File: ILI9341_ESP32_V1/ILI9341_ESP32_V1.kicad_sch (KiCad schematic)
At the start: 72 parts, among them J1 USB_C_Receptacle_USB2.0_16P, J2 Conn_01x02_Female, J3 Conn_01x02_Female, J4 Conn_01x18_Socket, Q1 BC807, SW1 SW_DIP_x01, SW10 SW_Push, SW11 SW_Push, SW12 SW_Push, SW13 SW_Wuerth_450301014042, SW2 SW_Push, SW3 SW_Push, SW4 SW_Push, SW5 SW_Push, SW6 SW_Push, SW7 SW_Push, SW8 SW_Push, SW9 SW_Push, U1 MCP73831-2-OT, U2 XM5062S, U3 ESP32-S3-WROOM-2, U4 3_2_ZOLL_ILI9341, U5 MAX98357AETE+T, U6 02FVS3, U7 02FVS3

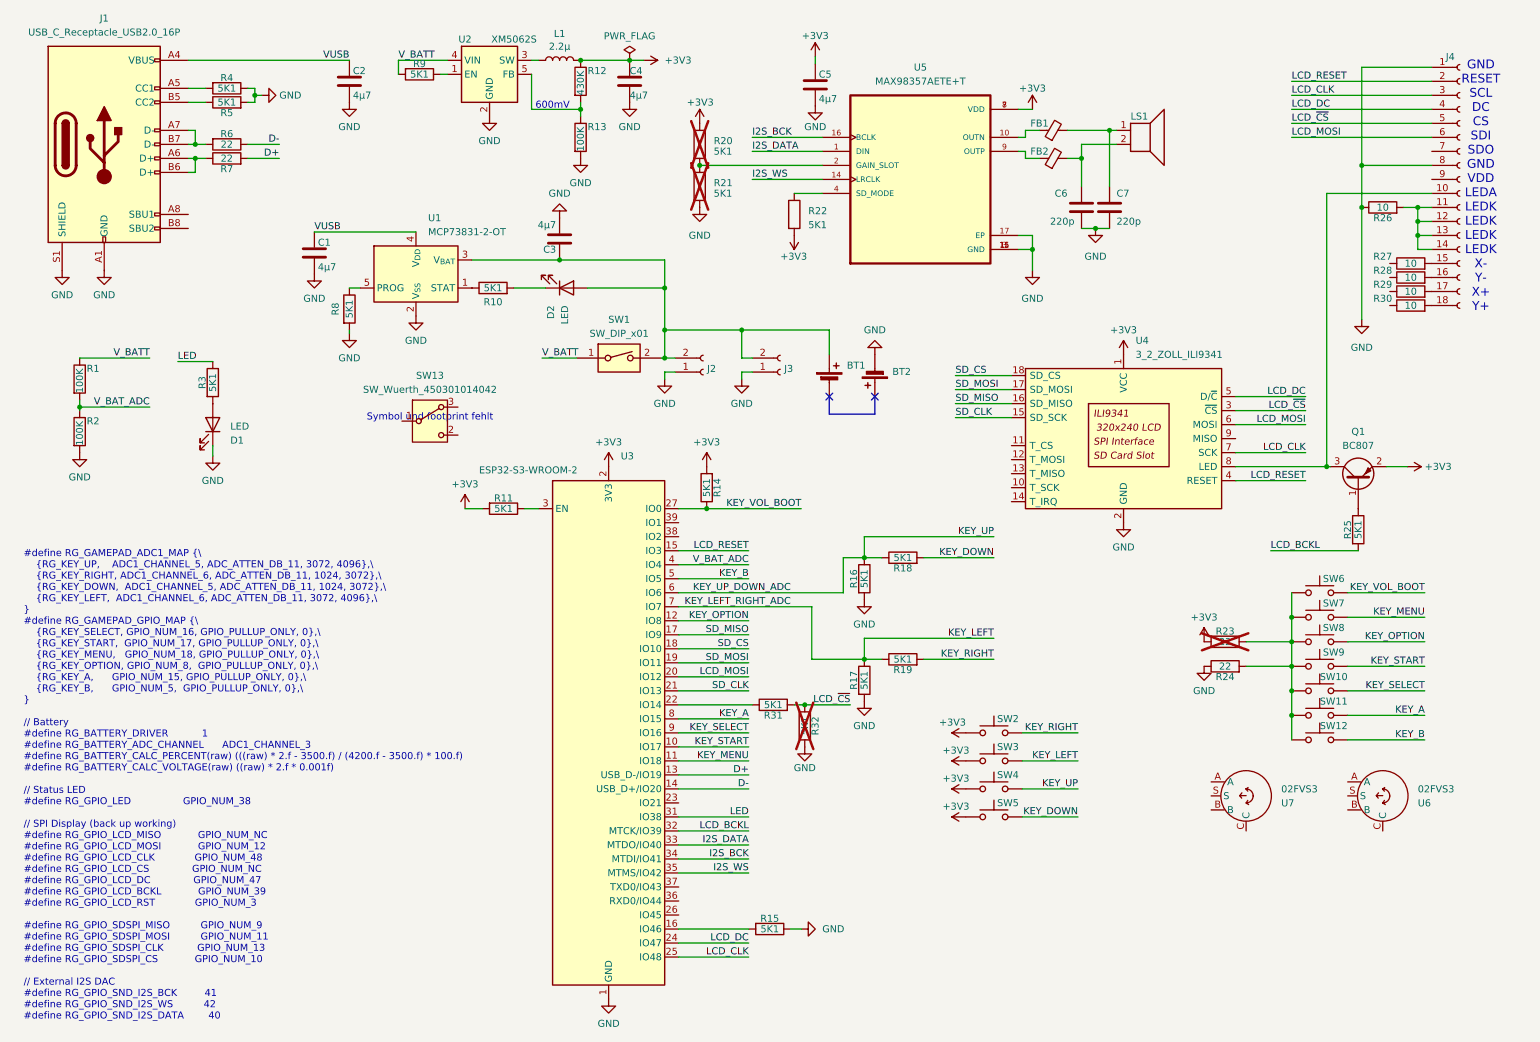
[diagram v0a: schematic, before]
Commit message: Add new connection (inter PCB)
build up new concept to fit in original gameboy case :) hope so
sound tested on prototyp wirering
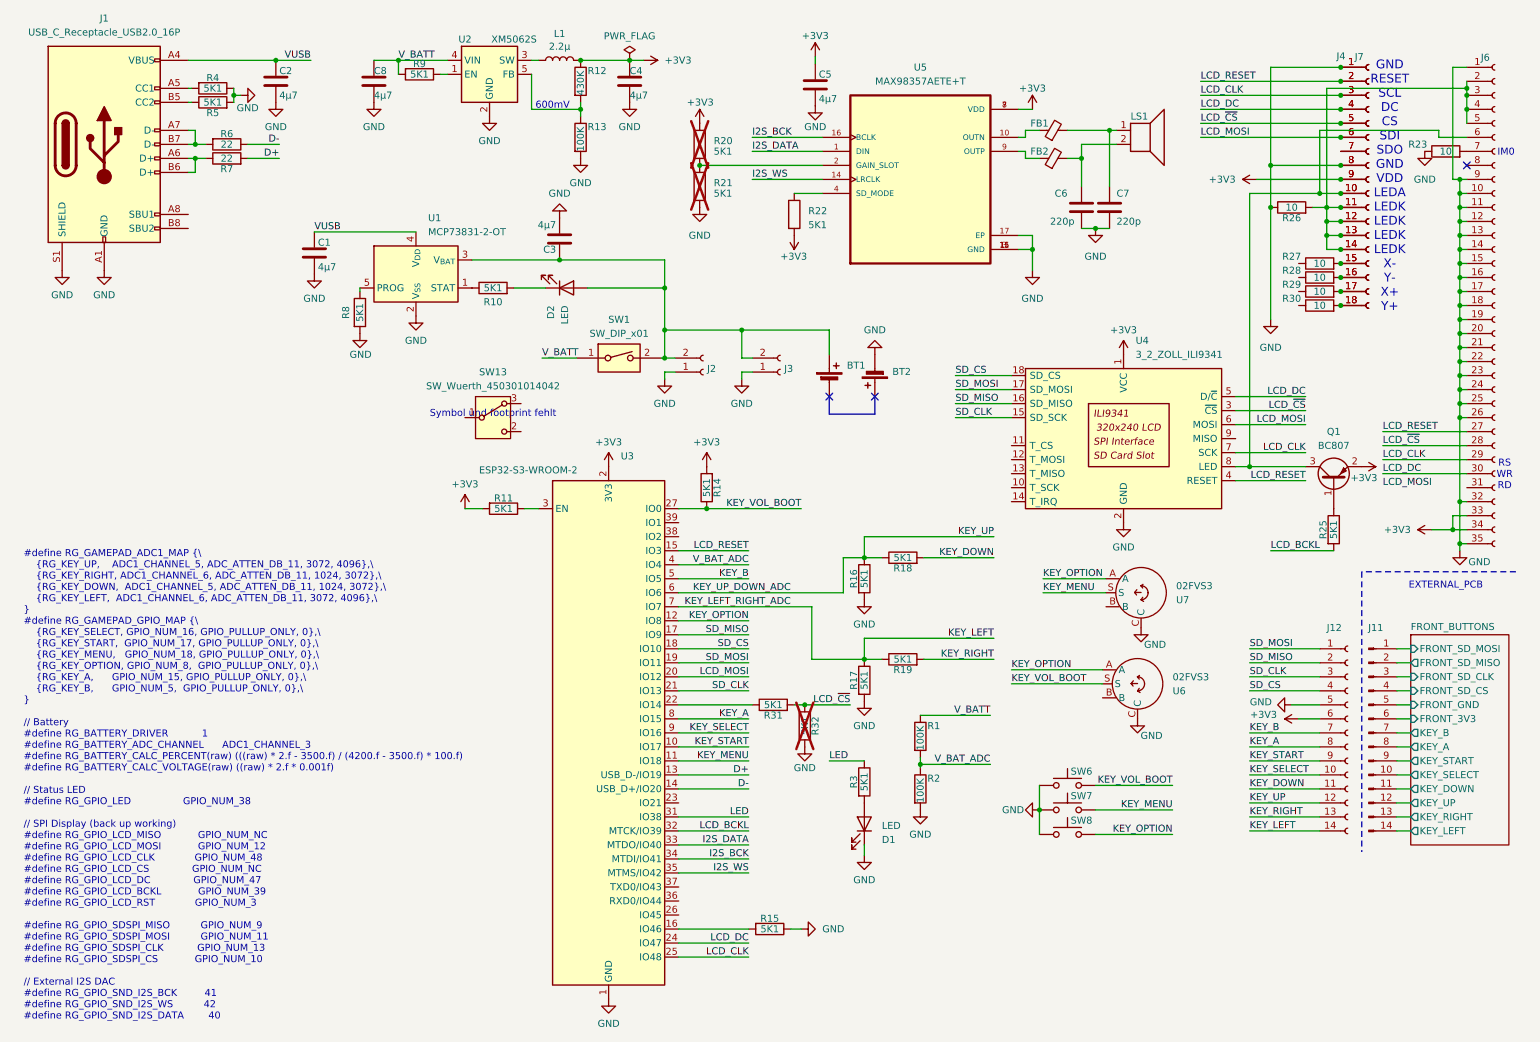
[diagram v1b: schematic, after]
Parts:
- removed R24: 22, Resistor_SMD:R_0603_1608Metric_Pad0.98x0.95mm_HandSolder, symbol Device:R
- removed SW10, SW11, SW12, SW2, SW3, SW4, SW5, SW9: SW_Push, TheBrutzlers_Lib:RubberpadButton_250µ_250µ, symbol Switch:SW_Push
- added C8: 4µ7, Capacitor_SMD:C_1206_3216Metric, symbol Device:C
- added J11: Conn_01x14_Pin, symbol Connector:Conn_01x14_Pin
- added J12: Conn_01x14_Socket, symbol Connector:Conn_01x14_Socket
- added J6: Conn_01x35_Socket, symbol Connector:Conn_01x35_Socket
- added J7: Conn_01x18_Socket, TheBrutzlers_Lib:solder connector 0.8mm 18 pin, symbol Connector:Conn_01x18_Socket
- LS1: LCSC (none) -> C391015
- R23: value 22 -> 10; now fitted; now in the parts list
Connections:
- net +3V3: now also J4.9 (Pin_9), J12.6 (Pin_6), J6.33 (Pin_33), J6.34 (Pin_34), J7.9 (Pin_9); no longer R23.2
- net GND: now also R23.1, SW6.1, SW7.1, SW8.1, U6.C, U7.C, C8.2, J12.5 (Pin_5), J6.1 (Pin_1), J6.10 (Pin_10), J6.11 (Pin_11), J6.12 (Pin_12), J6.13 (Pin_13), J6.14 (Pin_14), J6.15 (Pin_15), J6.16 (Pin_16), J6.17 (Pin_17), J6.18 (Pin_18), J6.19 (Pin_19), J6.20 (Pin_20), J6.21 (Pin_21), J6.22 (Pin_22), J6.23 (Pin_23), J6.24 (Pin_24), J6.25 (Pin_25), J6.26 (Pin_26), J6.32 (Pin_32), J6.35 (Pin_35), J6.9 (Pin_9), J7.1 (Pin_1), J7.8 (Pin_8)
- net KEY_A: now also J12.8 (Pin_8)
- net KEY_B: now also J12.7 (Pin_7)
- net KEY_DOWN: now also J12.11 (Pin_11)
- net KEY_LEFT: now also J12.14 (Pin_14)
- net KEY_MENU: now also U7.S
- net KEY_OPTION: now also U6.A, U7.A
- net KEY_RIGHT: now also J12.13 (Pin_13)
- net KEY_SELECT: now also J12.10 (Pin_10)
- net KEY_START: now also J12.9 (Pin_9)
- net KEY_UP: now also J12.12 (Pin_12)
- net KEY_VOL_BOOT: now also U6.S
- net LCD_CLK: now also J6.29 (Pin_29), J7.3 (Pin_3)
- net LCD_DC: now also J6.30 (Pin_30), J7.4 (Pin_4)
- net LCD_MOSI: now also J7.6 (Pin_6)
- net LCD_RESET: now also J6.27 (Pin_27), J7.2 (Pin_2)
- net LCD_~{CS}: now also J6.28 (Pin_28), J7.5 (Pin_5)
- net SD_CLK: now also J12.3 (Pin_3)
- net SD_CS: now also J12.4 (Pin_4)
- net SD_MISO: now also J12.2 (Pin_2)
- net SD_MOSI: now also J12.1 (Pin_1)
- net V_BATT: now also C8.1
- net at J4.10 (Pin_10), Q1.3 (C), U4.8 (LED): now also J6.6 (Pin_6), J7.10 (Pin_10)
- net at J4.18 (Pin_18), R30.2: now also J7.18 (Pin_18)
- net at J4.16 (Pin_16), R28.2: now also J7.16 (Pin_16)
- net at J4.11 (Pin_11), J4.12 (Pin_12), J4.13 (Pin_13)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: now also J6.2 (Pin_2), J6.3 (Pin_3), J6.4 (Pin_4), J6.5 (Pin_5), J7.11 (Pin_11), J7.12 (Pin_12), J7.13 (Pin_13), J7.14 (Pin_14)
- net at J4.17 (Pin_17), R29.2: now also J7.17 (Pin_17)
- net at J4.15 (Pin_15), R27.2: now also J7.15 (Pin_15)
- net at J4.7 (Pin_7): now also J7.7 (Pin_7)
- new net: J6.7 (Pin_7), R23.2
- new net FRONT_BUTTONS/FRONT_3V3: J11.6 (Pin_6)
- new net FRONT_BUTTONS/FRONT_GND: J11.5 (Pin_5)
- new net FRONT_BUTTONS/FRONT_SD_CLK: J11.3 (Pin_3)
- new net FRONT_BUTTONS/FRONT_SD_CS: J11.4 (Pin_4)
- new net FRONT_BUTTONS/FRONT_SD_MISO: J11.2 (Pin_2)
- new net FRONT_BUTTONS/FRONT_SD_MOSI: J11.1 (Pin_1)
- new net FRONT_BUTTONS/KEY_A: J11.8 (Pin_8)
- new net FRONT_BUTTONS/KEY_B: J11.7 (Pin_7)
- new net FRONT_BUTTONS/KEY_DOWN: J11.11 (Pin_11)
- new net FRONT_BUTTONS/KEY_LEFT: J11.14 (Pin_14)
- new net FRONT_BUTTONS/KEY_RIGHT: J11.13 (Pin_13)
- new net FRONT_BUTTONS/KEY_SELECT: J11.10 (Pin_10)
- new net FRONT_BUTTONS/KEY_START: J11.9 (Pin_9)
- new net FRONT_BUTTONS/KEY_UP: J11.12 (Pin_12)
- no-connect marks 2 -> 3
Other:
- added sheet FRONT_BUTTONS (FRONT_BUTTONS.kicad_sch)
- note added: "EXTERNAL_PCB"
- note added: "IM0"
- note added: "RS WR RD"
- moved on the sheet: C2, D1, J4, Q1, R1, R2, R25, R26, R27, R28, R29, R3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

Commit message: Update ESP from S3 to WROVER
Changed ESP to be compatible to odroid-go
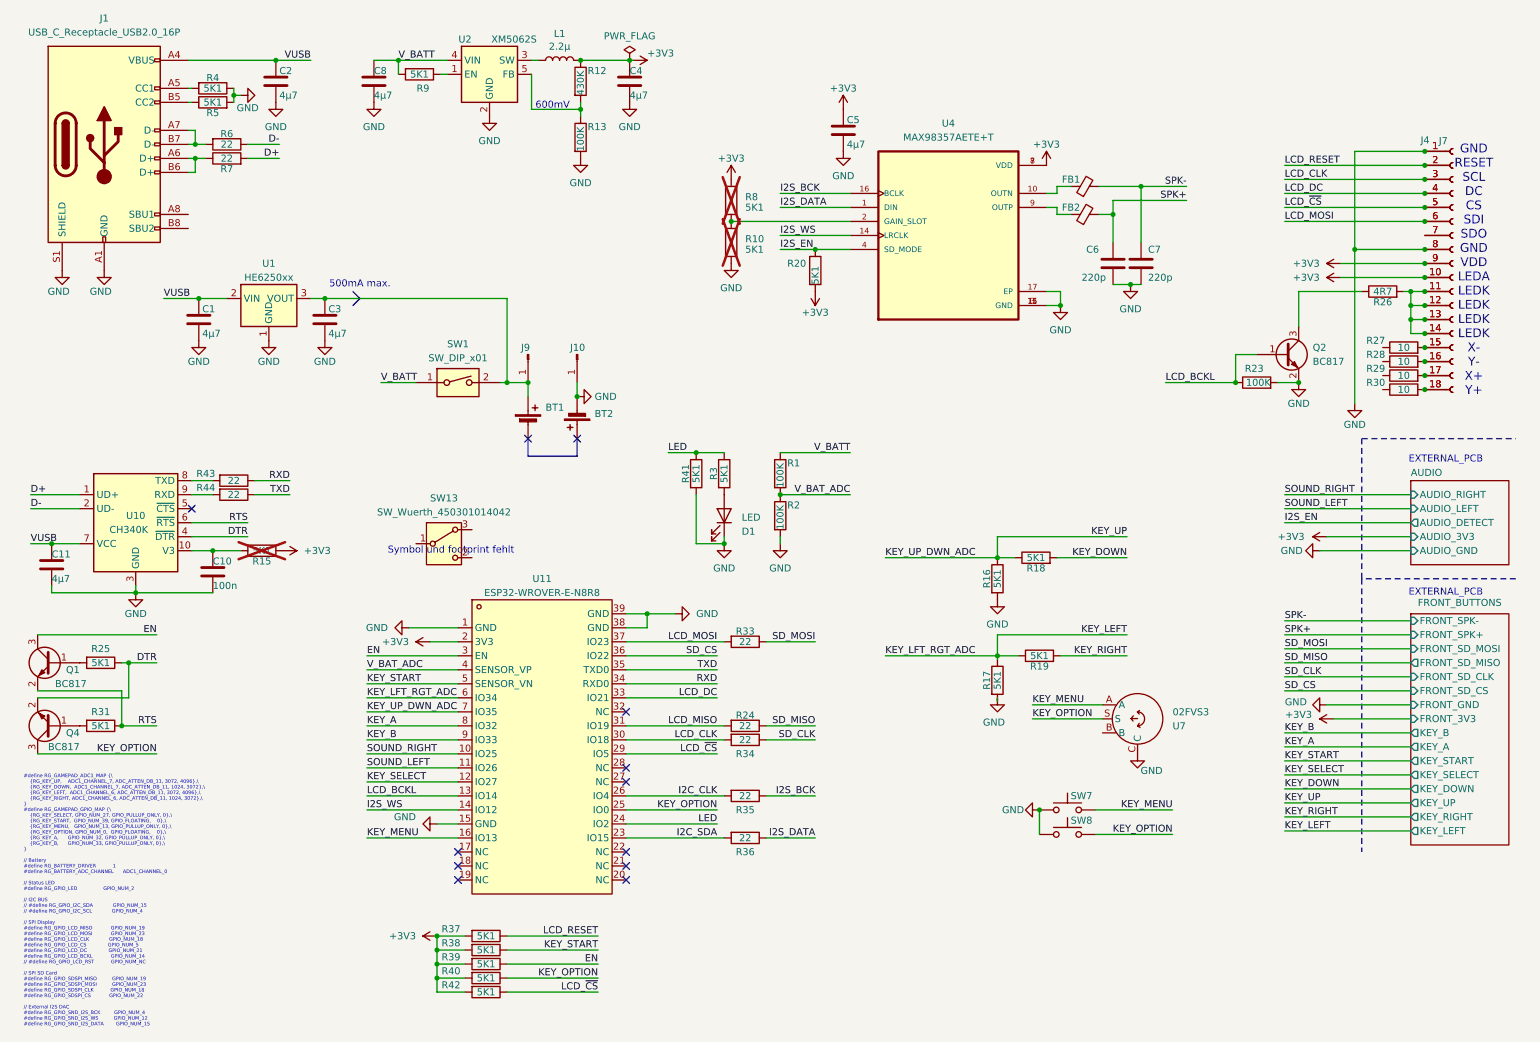
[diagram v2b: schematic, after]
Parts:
- removed D2: LED, LED_SMD:LED_0603_1608Metric, symbol Device:LED
- removed J11: Conn_01x14_Pin, symbol Connector:Conn_01x14_Pin
- removed J12: Conn_01x14_Socket, symbol Connector:Conn_01x14_Socket
- removed J2, J3: Conn_01x02_Female, Connector_JST:JST_PH_B2B-PH-K_1x02_P2.00mm_Vertical, symbol Connector:Conn_01x02_Female
- removed J6: Conn_01x35_Socket, symbol Connector:Conn_01x35_Socket
- removed LS1: Speaker, Connector_PinHeader_2.54mm:PinHeader_1x02_P2.54mm_Vertical, symbol Device:Speaker
- removed Q1: BC807, Package_TO_SOT_SMD:SOT-23, symbol Transistor_BJT:BC807
- removed R11, R14, R32: 5K1, Resistor_SMD:R_0603_1608Metric_Pad0.98x0.95mm_HandSolder, symbol Device:R
- removed R21, R22: 5K1, Resistor_SMD:R_0603_1608Metric, symbol Device:R
- removed SW6: SW_Push, TheBrutzlers_Lib:RubberpadButton_250µ_250µ, symbol Switch:SW_Push
- removed U1: MCP73831-2-OT, Package_TO_SOT_SMD:SOT-23-5, symbol Battery_Management:MCP73831-2-OT
- removed U3: ESP32-S3-WROOM-2, RF_Module:ESP32-S3-WROOM-2, symbol RF_Module:ESP32-S3-WROOM-2
- removed U4: 3_2_ZOLL_ILI9341, TheBrutzlers_Lib:ILI9341_3_2_ZOLL, symbol theBrutzler:3_2_ZOLL_ILI9341
- removed U5: MAX98357AETE+T, Package_DFN_QFN:QFN-16-1EP_3x3mm_P0.5mm_EP1.45x1.45mm, symbol MAX98357AETE_T:MAX98357AETE+T
- removed U6: 02FVS3, TheBrutzlers_Lib:02FVS3, symbol theBrutzler:02FVS3
- added C10: 100n, Capacitor_SMD:C_1206_3216Metric, symbol Device:C
- added C11: 4µ7, Capacitor_SMD:C_1206_3216Metric, symbol Device:C
- added J10: Conn_01x01_Pin, TheBrutzlers_Lib:NINTENDO_MINUS, symbol Connector:Conn_01x01_Pin
- added J9: Conn_01x01_Pin, TheBrutzlers_Lib:NINTENDO_PLUS, symbol Connector:Conn_01x01_Pin
- added Q1, Q2, Q4: BC817, Package_TO_SOT_SMD:SOT-23, symbol Transistor_BJT:BC817
- added R24, R33, R34, R35, R36, R43, R44: 22, Resistor_SMD:R_0603_1608Metric_Pad0.98x0.95mm_HandSolder, symbol Device:R
- added R37, R38, R39, R40, R41, R42: 5K1, Resistor_SMD:R_0603_1608Metric_Pad0.98x0.95mm_HandSolder, symbol Device:R
- added U1: HE6250xx, Package_TO_SOT_SMD:SOT-89-3, symbol Regulator_Linear:HT75xx-1-SOT89
- added U10: CH340K, TheBrutzlers_Lib:SSOP-10_3.9x4.9mm_P1.00mm_EP_3mmx2mm, symbol theBrutzler:CH340K
- added U11: ESP32-WROVER-E-N8R8, easyeda2kicad:WIFI-SMD_ESP32-WROVER-IE8MB, symbol easyeda2kicad:ESP32-WROVER-E-N8R8
- added U4: MAX98357AETE+T, Package_DFN_QFN:QFN-16-1EP_3x3mm_P0.5mm_EP1.45x1.45mm, symbol MAX98357AETE_T:MAX98357AETE+T
- R10, R8: footprint Resistor_SMD:R_0603_1608Metric_Pad0.98x0.95mm_HandSolder -> Resistor_SMD:R_0603_1608Metric; LCSC (none) -> C26000; now not fitted; now left out of the parts list
- R15: now not fitted; now left out of the parts list
- R20: now fitted; now in the parts list
- R23: value 10 -> 100K
- R26: value 10 -> 4R7
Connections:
- net +3V3: now also J4.10 (Pin_10), J7.10 (Pin_10), R15.2, R20.2, R8.1, R37.2, R38.2, R39.2, R40.2, R42.2, U11.2 (3V3), U4.7 (VDD), U4.8 (VDD); no longer R20.1
- net D+: now also U10.1 (UD+)
- net D-: now also U10.2 (UD-)
- net GND: now also R10.2, R23.2, C10.2, C11.2, J10.1 (Pin_1), Q2.2 (E), R41.2, U1.1 (GND), U10.3 (GND), U10.PAD (GND), U11.1 (GND), U11.15 (GND), U11.38 (GND), U11.39 (GND), U4.11 (GND), U4.15 (GND), U4.17 (EP), U4.3 (GND); no longer R15.1, R23.1, R26.1, R8.2
- net I2S_BCK: now also R35.1, U4.16 (BCLK)
- net I2S_DATA: now also R36.1, U4.1 (DIN)
- net I2S_WS: now also U11.14 (IO12), U4.14 (LRCLK)
- net KEY_A: now also U11.8 (IO32)
- net KEY_B: now also U11.9 (IO33)
- net KEY_LEFT: now also U11.6 (IO34)
- net KEY_MENU: now also U7.A, U11.16 (IO13); no longer U7.S
- net KEY_OPTION: now also U7.S, Q4.3 (C), R40.1, U11.25 (IO0); no longer U7.A
- net KEY_SELECT: now also U11.12 (IO27)
- net KEY_START: now also R38.1, U11.5 (SENSOR_VN)
- net KEY_UP: now also U11.7 (IO35)
- net LCD_BCKL: now also R23.1, Q2.1 (B), U11.13 (IO14); no longer R25.2
- net LCD_CLK: now also R34.2, U11.30 (IO18)
- net LCD_DC: now also U11.33 (IO21)
- net LCD_MOSI: now also R33.2, U11.37 (IO23)
- net LCD_RESET: now also R37.1
- net LCD_~{CS}: now also R42.1, U11.29 (IO5); no longer R31.2
- net LED: now also R41.1, U11.24 (IO2)
- net SD_CLK: now also R34.1
- net SD_CS: now also U11.36 (IO22)
- net SD_MISO: now also R24.1
- net SD_MOSI: now also R33.1
- net VUSB: now also C11.1, U1.2 (VIN), U10.7 (VCC)
- net V_BAT_ADC: now also U11.4 (SENSOR_VP)
- net SPK-: now reaches C7.2, FB1.2
- net SPK+: now reaches C6.1, FB2.2
- net at BT1.1 (+), C3.1, SW1.2: now also J9.1 (Pin_1), U1.3 (VOUT)
- net at FB2.1: now also U4.9 (OUTP)
- net DTR: now reaches R25.1
- net DTR: now also Q4.2 (E), U10.4 (~{DTR})
- net at R10.1: now also R8.2, U4.2 (GAIN_SLOT)
- net at FB1.1: now also U4.10 (OUTN)
- net RTS: now reaches R31.1
- net RTS: now also Q1.2 (E), U10.6 (~{RTS})
- new net: R44.2, U10.9 (RXD)
- new net: Q4.1 (B), R31.2
- new net: Q2.3 (C), R26.1
- new net: R43.2, U10.8 (TXD)
- new net: C10.1, R15.1, U10.10 (V3)
- new net: Q1.1 (B), R25.2
- new net EN: Q1.3 (C), R39.1, U11.3 (EN)
- new net I2C_CLK: R35.2, U11.26 (IO4)
- new net I2C_SDA: R36.2, U11.23 (IO15)
- new net I2S_EN: R20.1, U4.4 (SD_MODE)
- new net LCD_MISO: R24.2, U11.31 (IO19)
- new net RXD: R43.1, U11.34 (RXD0)
- new net SOUND_LEFT: U11.11 (IO26)
- new net SOUND_RIGHT: U11.10 (IO25)
- new net TXD: R44.1, U11.35 (TXD0)
- no-connect marks 3 -> 12
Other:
- added sheet AUDIO (AUDIO.kicad_sch)
- sheet FRONT_BUTTONS ports: added FRONT_SPK+, FRONT_SPK-; removed none
- note added: "#define RG_GAMEPAD_ADC1_MAP {\ {RG_KEY_UP, ADC1_CHANNEL_7, ADC_ATTEN_DB_11, 3072, 4096},\ {RG_KEY_DOWN, ADC1_CHANNEL_7, ADC_ATTEN_DB_11, 1024, 3072},\ {RG_KEY_LEFT, ADC1_CHANNEL_6, ADC_ATTEN_DB_11, 3072, 4096},\ {RG_KEY_RIGHT, ADC1_CHANNEL_6, ADC_ATTEN_DB_11, 1024, 3072},\ } #define RG_GAMEPAD_GPIO_MAP {\ {RG_KEY_SELECT, GPIO_NUM_27, GPIO_PULLUP_ONLY, 0},\ {RG_KEY_START, GPIO_NUM_39, GPIO_FLOATIN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"
- note added: "500mA max."
- note removed: "#define RG_GAMEPAD_ADC1_MAP {\ {RG_KEY_UP, ADC1_CHANNEL_5, ADC_ATTEN_DB_11, 3072, 4096},\ {RG_KEY_RIGHT, ADC1_CHANNEL_6, ADC_ATTEN_DB_11, 1024, 3072},\ {RG_KEY_DOWN, ADC1_CHANNEL_5, ADC_ATTEN_DB_11, 1024, 3072},\ {RG_KEY_LEFT, ADC1_CHANNEL_6, ADC_ATTEN_DB_11, 3072, 4096},\ } #define RG_GAMEPAD_GPIO_MAP {\ {RG_KEY_SELECT, GPIO_NUM_16, GPIO_PULLUP_ONLY, 0},\ {RG_KEY_START, GPIO_NUM_17, GPIO_PULLUP_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"
- note removed: "IM0"
- note removed: "RS WR RD"
- moved on the sheet: BT1, BT2, C1, C3, D1, J4, J7, R1, R16, R17, R18, R19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
